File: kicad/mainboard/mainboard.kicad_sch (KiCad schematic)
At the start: 33 parts, among them J1 USB_C_Receptacle_USB2.0_16P, J2 Conn_01x06_Socket, J3 Conn_01x07_Socket, J4 Conn_01x03_Socket, J5 Conn_01x07_Socket, SW1 FSM2JSMAATR, SW2 FSM2JSMAATR, U1 TPD1E05U06DYA, U2 TPD1E05U06DYA, U3 ESP32-S3-WROOM-1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

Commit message: mainboard pcb v1
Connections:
- net +5V: now also J4.3 (Pin_3); no longer J4.1 (Pin_1)
- net EN: now also C6.2, SW1.1; no longer C6.1, SW1.3
- net GND: now also C6.1, C7.1, SW1.3, SW2.3; no longer C6.2, C7.2, SW1.1, SW2.1
- net GPIO0: now also C7.2, SW2.1; no longer C7.1, SW2.3
- net LED_DATA: now also J4.1 (Pin_1), U3.28 (SPIIO6/GPIO35/FSPID/SUBSPID); no longer J4.3 (Pin_3), U3.15 (GPIO3/TOUCH3/ADC1_CH2)
- no-connect marks 30 -> 29
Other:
- moved on the sheet: C6, C7, SW1, SW2

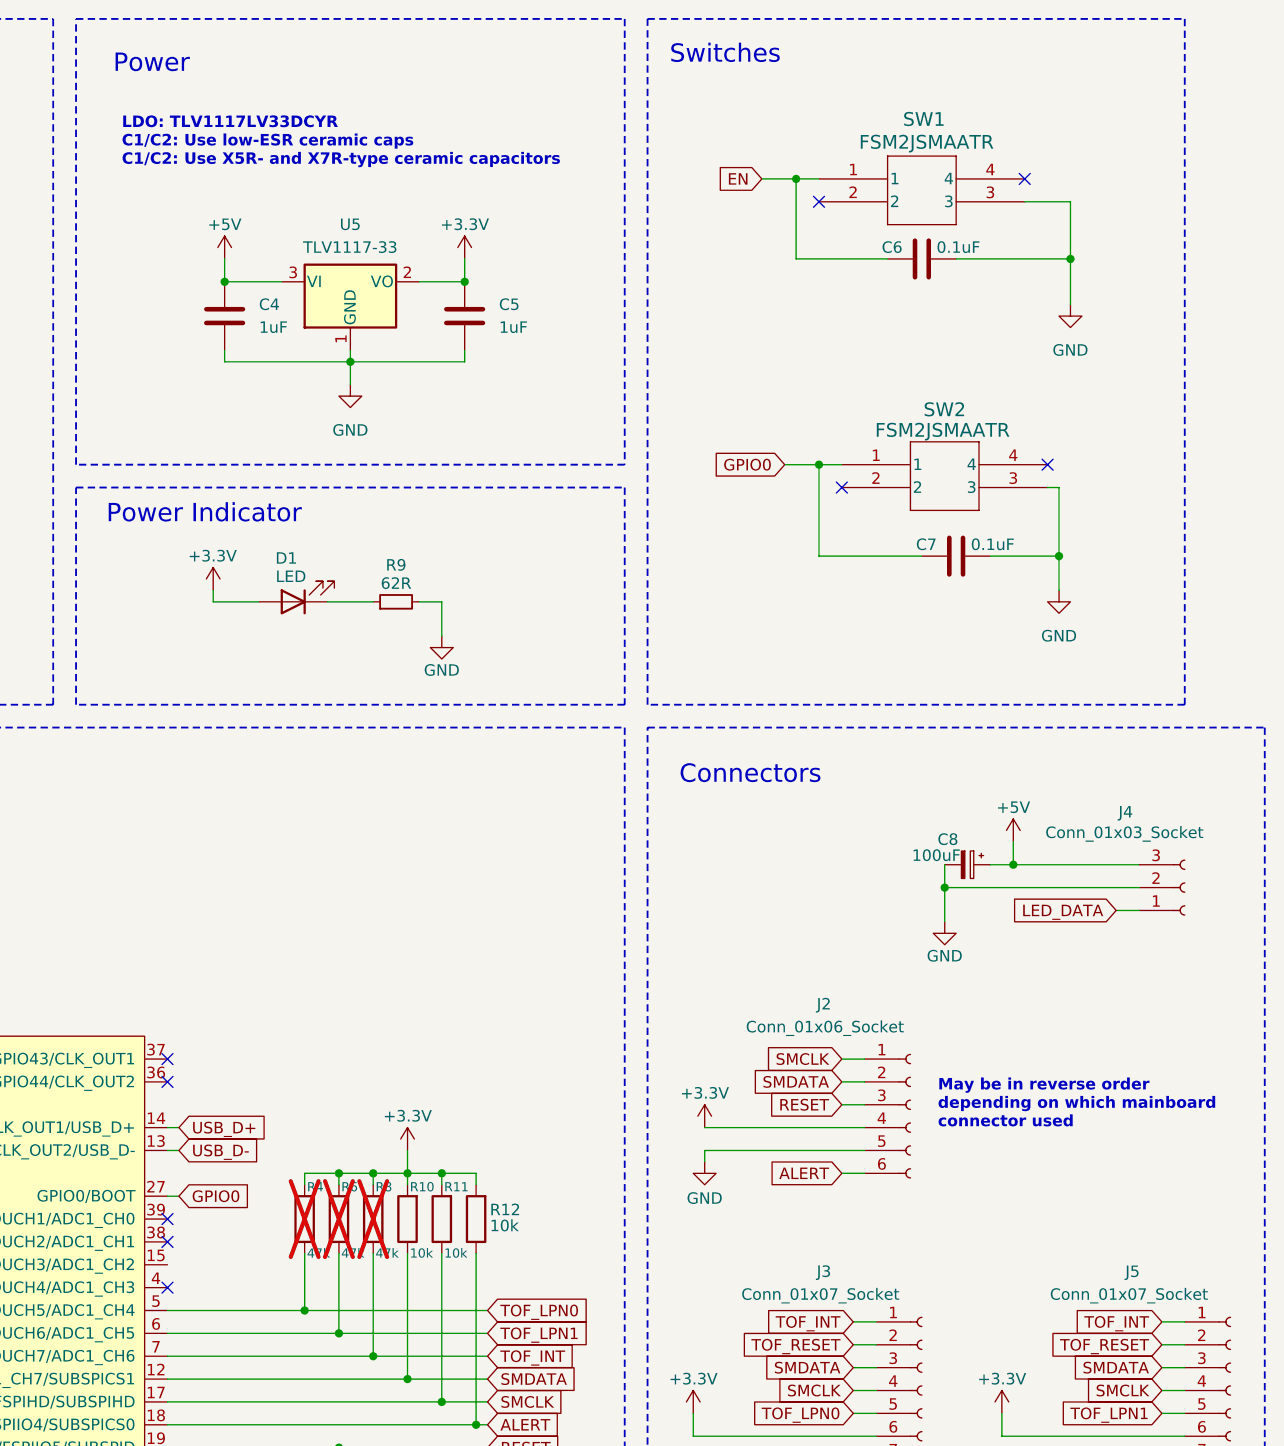
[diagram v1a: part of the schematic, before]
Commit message: mainboard cleaned
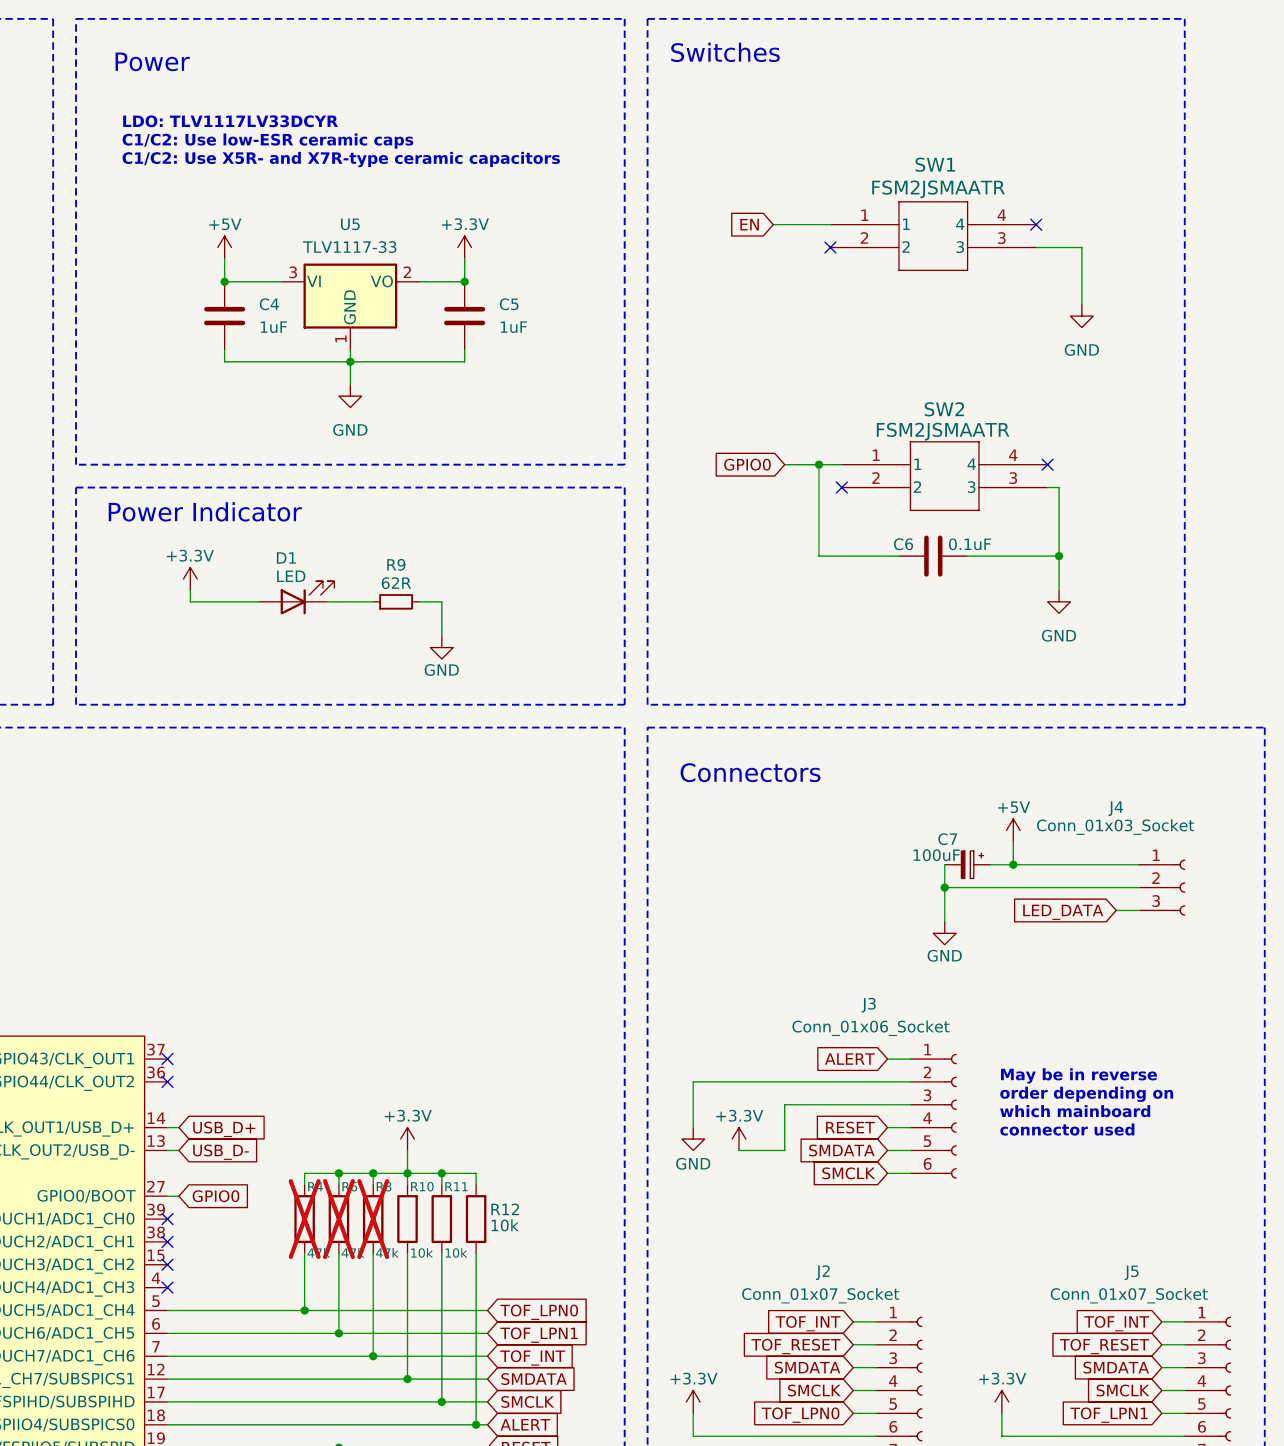
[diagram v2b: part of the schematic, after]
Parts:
- removed C6: 0.1uF, Capacitor_SMD:C_0805_2012Metric_Pad1.18x1.45mm_HandSolder, symbol Device:C
- renumbered C7 to C6, C8 to C7, J3 to J2, J2 to J3
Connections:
- net +3.3V: now also J3.3 (Pin_3); no longer J3.4 (Pin_4)
- net +5V: now also J4.1 (Pin_1); no longer J4.3 (Pin_3)
- net ALERT: now also J3.1 (Pin_1); no longer J3.6 (Pin_6)
- net GND: now also J3.2 (Pin_2); no longer J3.5 (Pin_5)
- net LED_DATA: now also J4.3 (Pin_3); no longer J4.1 (Pin_1)
- net RESET: now also J3.4 (Pin_4); no longer J3.3 (Pin_3)
- net SMCLK: now also J3.6 (Pin_6); no longer J3.1 (Pin_1)
- net SMDATA: now also J3.5 (Pin_5); no longer J3.2 (Pin_2)
- no-connect marks 29 -> 30
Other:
- moved on the sheet: C6, J3, SW1

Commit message: add mountholes
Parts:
- added H1, H2, H3, H4: MountingHole, MountingHole:MountingHole_2.2mm_M2, symbol Mechanical:MountingHole
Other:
- note added: "Mounting holes"

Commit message: remove buttons
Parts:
- C6, SW1, SW2: now not fitted
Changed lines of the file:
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@@
 	(text "May be in reverse\norder depending on\nwhich mainboard\nconnector used"
 		(exclude_from_sim no)
-		(at 224.536 135.89 0)
+		(at 231.14 135.636 0)
 		(effects
 			(font
@@
 		(exclude_from_sim no)
 		(in_bom yes)
-		(on_board yes)
-		(dnp no)
+		(on_board no)
+		(dnp yes)
 		(property "Reference" "SW2"
 			(at 218.44 58.674 0)
@@
 		(exclude_from_sim no)
 		(in_bom yes)
-		(on_board yes)
-		(dnp no)
+		(on_board no)
+		(dnp yes)
 		(property "Reference" "C6"
 			(at 213.868 73.66 90)
@@
 		(exclude_from_sim no)
 		(in_bom yes)
-		(on_board yes)
-		(dnp no)
+		(on_board no)
+		(dnp yes)
 		(property "Reference" "SW1"
 			(at 217.424 31.496 0)

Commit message: remove switches
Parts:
- removed C6: 0.1uF, Capacitor_SMD:C_0805_2012Metric_Pad1.18x1.45mm_HandSolder, symbol Device:C
- removed SW1, SW2: FSM2JSMAATR, FSM2JSMAATR:SWITCH_FSM2JSMAA_TYC, symbol FSM2JSMAATR:FSM2JSMAATR
- renumbered C7 to C6
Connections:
- net EN: no longer names the net of C1.1, R1.1, U3.3 (EN)
- net GPIO0: no longer names the net of U3.27 (GPIO0/BOOT)
- no-connect marks 30 -> 27
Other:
- note removed: "Switches"
- moved on the sheet: C6, H1, H2, H3, H4, J2, J3, J4, J5

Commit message: fixup stuff
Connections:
- net +5V: now also J4.2 (Pin_2); no longer J4.1 (Pin_1)
- net GND: now also J4.3 (Pin_3); no longer J4.2 (Pin_2)
- net LED_DATA: now also J4.1 (Pin_1); no longer J4.3 (Pin_3)
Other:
- moved on the sheet: C6
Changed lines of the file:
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@@
 	)
 	(junction
-		(at 218.44 33.02)
+		(at 154.94 143.51)
 		(diameter 0)
 		(color 0 0 0 0)
 	)
 	(junction
-		(at 154.94 143.51)
+		(at 71.12 78.74)
 		(diameter 0)
 		(color 0 0 0 0)
 	)
 	(junction
-		(at 71.12 78.74)
+		(at 229.87 38.1)
 		(diameter 0)
 		(color 0 0 0 0)
@@
 	)
 	(junction
+		(at 223.52 33.02)
+		(diameter 0)
+		(color 0 0 0 0)
+	)
+	(junction
 		(at 52.07 78.74)
 		(diameter 0)
@@
 	)
 	(junction
-		(at 226.06 30.48)
-		(diameter 0)
-		(color 0 0 0 0)
-	)
-	(junction
 		(at 63.5 78.74)
 		(diameter 0)
@@
 	(wire
 		(pts
-			(xy 218.44 36.83) (xy 218.44 33.02)
+			(xy 229.87 39.37) (xy 229.87 38.1)
 		)
 		(stroke
@@
 	(wire
 		(pts
-			(xy 165.1 52.07) (xy 165.1 53.34)
+			(xy 240.03 35.56) (xy 229.87 35.56)
 		)
 		(stroke
@@
 	(wire
 		(pts
-			(xy 165.1 53.34) (xy 152.4 53.34)
+			(xy 165.1 52.07) (xy 165.1 53.34)
 		)
 		(stroke
@@
 	(wire
 		(pts
-			(xy 132.08 171.45) (xy 166.37 171.45)
+			(xy 165.1 53.34) (xy 152.4 53.34)
 		)
 		(stroke
@@
 	(wire
 		(pts
-			(xy 52.07 63.5) (xy 52.07 78.74)
+			(xy 132.08 171.45) (xy 166.37 171.45)
 		)
 		(stroke
@@
 	(wire
 		(pts
-			(xy 190.5 91.44) (xy 190.5 93.98)
+			(xy 52.07 63.5) (xy 52.07 78.74)
 		)
 		(stroke
@@
 	(wire
 		(pts
-			(xy 242.57 81.28) (xy 245.11 81.28)
+			(xy 190.5 91.44) (xy 190.5 93.98)
 		)
 		(stroke
@@
 	(wire
 		(pts
-			(xy 132.08 168.91) (xy 162.56 168.91)
+			(xy 242.57 81.28) (xy 245.11 81.28)
 		)
 		(stroke
@@
 	(wire
 		(pts
-			(xy 218.44 33.02) (xy 240.03 33.02)
+			(xy 132.08 168.91) (xy 162.56 168.91)
 		)
 		(stroke
@@
 	(wire
 		(pts
+			(xy 223.52 33.02) (xy 240.03 33.02)
+		)
+		(stroke
+			(width 0)
+			(type default)
+		)
+	)
+	(wire
+		(pts
 			(xy 49.53 41.91) (xy 83.82 41.91)
 		)
@@
 	(wire
 		(pts
-			(xy 237.49 35.56) (xy 240.03 35.56)
-		)
-		(stroke
-			(width 0)
-			(type default)
-		)
-	)
-	(wire
-		(pts
 			(xy 151.13 187.96) (xy 151.13 186.69)
 		)
@@
 	(wire
 		(pts
-			(xy 147.32 144.78) (xy 147.32 143.51)
+			(xy 229.87 35.56) (xy 229.87 38.1)
 		)
 		(stroke
@@
 	(wire
 		(pts
-			(xy 226.06 27.94) (xy 226.06 30.48)
+			(xy 147.32 144.78) (xy 147.32 143.51)
 		)
 		(stroke
@@
 	(wire
 		(pts
-			(xy 218.44 30.48) (xy 218.44 33.02)
-		)
-		(stroke
-			(width 0)
-			(type default)
-		)
-	)
-	(wire
-		(pts
-			(xy 223.52 30.48) (xy 226.06 30.48)
+			(xy 58.42 30.48) (xy 58.42 34.29)
 		)
 		(stroke
@@
 	(wire
 		(pts
-			(xy 58.42 30.48) (xy 58.42 34.29)
+			(xy 69.85 114.3) (xy 76.2 114.3)
 		)
 		(stroke
@@
 	(wire
 		(pts
-			(xy 69.85 114.3) (xy 76.2 114.3)
+			(xy 237.49 30.48) (xy 240.03 30.48)
 		)
 		(stroke
@@
 	(wire
 		(pts
-			(xy 40.64 78.74) (xy 52.07 78.74)
+			(xy 223.52 38.1) (xy 229.87 38.1)
 		)
 		(stroke
@@
 	(wire
 		(pts
-			(xy 226.06 30.48) (xy 240.03 30.48)
+			(xy 40.64 78.74) (xy 52.07 78.74)
 		)
 		(stroke
@@
 	(wire
 		(pts
+			(xy 223.52 29.21) (xy 223.52 33.02)
+		)
+		(stroke
+			(width 0)
+			(type default)
+		)
+	)
+	(wire
+		(pts
 			(xy 83.82 78.74) (xy 86.36 78.74)
 		)
@@
 	(global_label "LED_DATA"
 		(shape input)
-		(at 237.49 35.56 180)
+		(at 237.49 30.48 180)
 		(fields_autoplaced yes)
 		(effects
@@
 		)
 		(property "Intersheetrefs" "${INTERSHEET_REFS}"
-			(at 225.6753 35.56 0)
+			(at 225.6753 30.48 0)
 			(effects
 				(font
@@
 	(symbol
 		(lib_id "power:+5V")
-		(at 226.06 27.94 0)
+		(at 223.52 29.21 0)
 		(mirror y)
 		(unit 1)
@@
 		(dnp no)
 		(property "Reference" "#PWR021"
-			(at 226.06 31.75 0)
+			(at 223.52 33.02 0)
 			(effects
 				(font
@@
 		)
 		(property "Value" "+5V"
-			(at 226.06 24.13 0)
+			(at 223.52 25.4 0)
 			(effects
 				(font
@@
 		)
 		(property "Footprint" ""
-			(at 226.06 27.94 0)
+			(at 223.52 29.21 0)
 			(effects
 				(font
@@
 		)
 		(property "Datasheet" ""
-			(at 226.06 27.94 0)
+			(at 223.52 29.21 0)
 			(effects
 				(font
@@
 		)
 		(property "Description" "Power symbol creates a global label with name \"+5V\""
-			(at 226.06 27.94 0)
+			(at 223.52 29.21 0)
 			(effects
 				(font
@@
 	(symbol
 		(lib_id "Device:C_Polarized_Small")
-		(at 220.98 30.48 270)
+		(at 223.52 35.56 0)
 		(unit 1)
 		(exclude_from_sim no)
@@
 		(dnp no)
 		(property "Reference" "C6"
-			(at 219.964 27.686 90)
+			(at 221.234 33.782 0)
 			(effects
 				(font
@@
 		)
 		(property "Value" "100uF"
-			(at 220.218 29.464 90)
+			(at 221.234 35.814 0)
 			(effects
 				(font
@@
 		)
 		(property "Footprint" "Capacitor_SMD:CP_Elec_6.3x5.8"
-			(at 220.98 30.48 0)
+			(at 223.52 35.56 0)
 			(effects
 				(font
@@
 		)
 		(property "Datasheet" "~"
-			(at 220.98 30.48 0)
+			(at 223.52 35.56 0)
 			(effects
 				(font
@@
 		)
 		(property "Description" "Polarized capacitor, small symbol"
-			(at 220.98 30.48 0)
+			(at 223.52 35.56 0)
 			(effects
 				(font
@@
 	(symbol
 		(lib_id "power:GND")
-		(at 218.44 36.83 0)
+		(at 229.87 39.37 0)
 		(unit 1)
 		(exclude_from_sim no)
@@
 		(dnp no)
 		(property "Reference" "#PWR019"
-			(at 218.44 43.18 0)
+			(at 229.87 45.72 0)
 			(effects
 				(font
@@
 		)
 		(property "Value" "GND"
-			(at 218.44 40.64 0)
+			(at 229.87 43.18 0)
 			(effects
 				(font
@@
 		)
 		(property "Footprint" ""
-			(at 218.44 36.83 0)
+			(at 229.87 39.37 0)
 			(effects
 				(font
@@
 		)
 		(property "Datasheet" ""
-			(at 218.44 36.83 0)
+			(at 229.87 39.37 0)
 			(effects
 				(font
@@
 		)
 		(property "Description" "Power symbol creates a global label with name \"GND\" , ground"
-			(at 218.44 36.83 0)
+			(at 229.87 39.37 0)
 			(effects
 				(font
